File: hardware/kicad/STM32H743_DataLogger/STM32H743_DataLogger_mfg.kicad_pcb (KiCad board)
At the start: 4 copper layers, 160 x 100 mm, 228 parts, among them J1 24VDC_Input, J10 SWD_Debug, J11 USB-C, J12 UART_Debug, J13 BOOT0_Select, J14 TC2050-IDC, J20 AI_CH0, J21 AI_CH1, J22 AI_CH2, J23 AI_CH3, J30 DI_0, J31 DI_1, J32 DI_2, J33 DI_3, J34 DI_4, J35 DI_5, J36 DI_6, J37 DI_7, J40 DO_0, J41 DO_1, J42 DO_2, J43 DO_3, J50 RS485, J51 CAN, J60 J0011D21BNL, J70 SMA_LoRa, J71 U.FL_WiFi, J72 NanoSIM, J73 SMA_LTE, J74 SMA_GNSS, J80 microSD, K1 HF46F-G/5-HS1T, K2 HF46F-G/5-HS1T, K3 HF46F-G/5-HS1T, K4 HF46F-G/5-HS1T, Q1 SI4435DDY, U1 TPS54560, U10 STM32H743VIT6, U2 TLV1117LV33, U20 OPA2376, U21 OPA2376, U3 TPS7A4533, U30 TLP293, U31 ULN2003A, U32 TLP293, U33 TLP293, U34 TLP293, U35 TLP293, U36 TLP293, U37 TLP293, U38 TLP293, U40 ISO3082, U41 ISO1042, U42 NXJ1S0505MC, U43 NXJ1S0505MC, U50 W5500, U60 SX1276, U61 ATWINC1500, U62 SIM7600G-H, U62B RN4870, U63 TPS73641, U64 TPS3823-33, U70 W25Q64JV, U71 AT24C256C, Y1 25MHz, Y2 32.768kHz, Y3 25MHz, Y4 32MHz

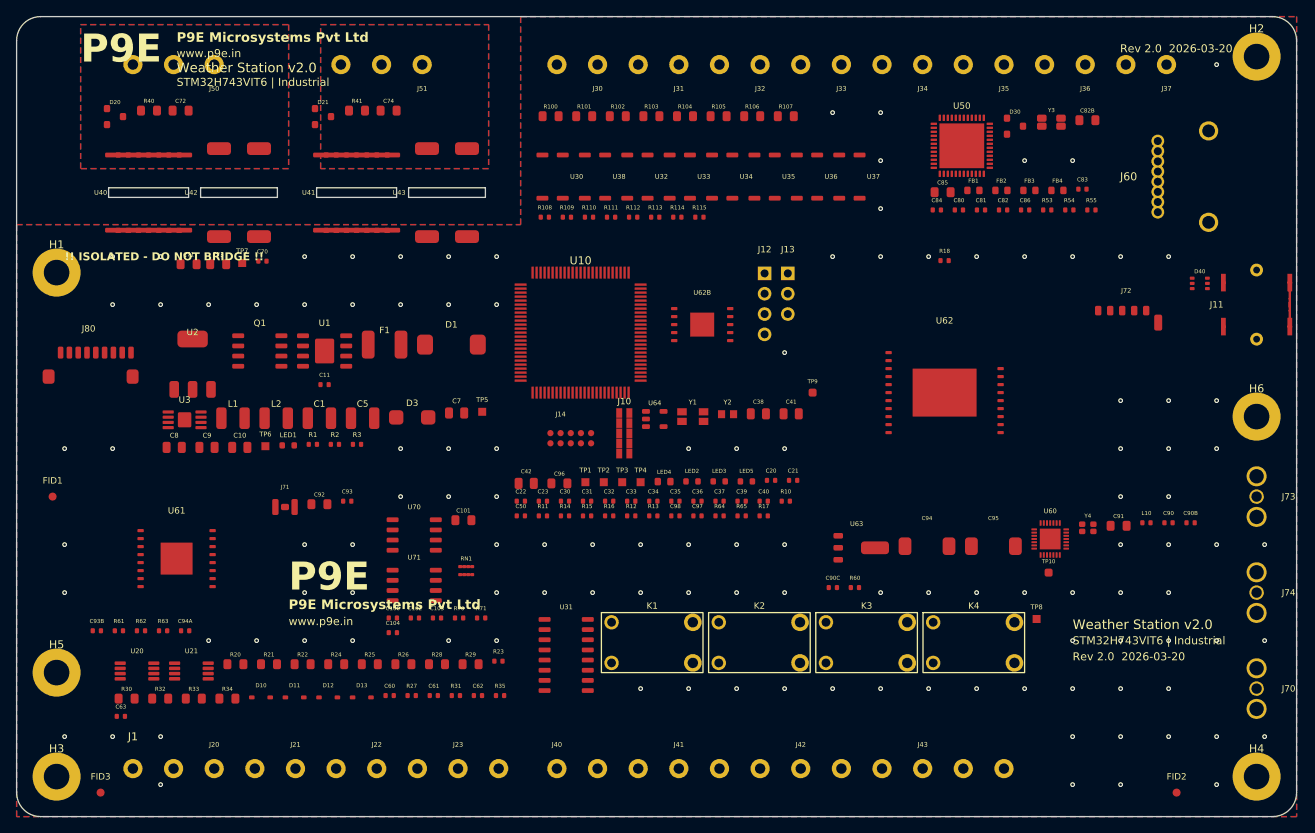
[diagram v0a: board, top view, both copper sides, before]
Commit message: Import the autorouted session; 84% of connections, verified independently
Built a Specctra DSN exporter and a session importer, routed the board
with freerouting, and imported the result: 1520 tracks and 303 vias on
F.Cu / In2.Cu / B.Cu, with In1.Cu left as an unbroken ground plane.

Getting there took three format fixes worth recording. The DSN declared
(resolution um 10) but coordinates were scaled mm->um, so the router saw a
16x10mm board and could place almost nothing; %g emitted scientific
notation for large coordinates, which the parser rejected; and the session
comes back at 100000 units/mm rather than the 10000 the DSN uses, which
imported every track 10x oversized until it was caught by comparing a
track endpoint against its pad.

Via size turned out to be the real routing constraint: at 0.6mm the
autorouter could not stagger a fanout into the 0.5mm-pitch LQFP-100 and
completed under half the board. At 0.45mm/0.25mm with 0.125mm clearance it
gets much further.

Do not trust the router's own completion figure. Freerouting reported "3
unrouted" for this session; walking each net's pads against the imported
copper shows many MCU pins never reached. The real figure is 271 of 322
connections (84%) - 110 nets complete, 35 partial, 10 untouched - and the
45 nets needing work are listed in docs/unrouted_nets.txt.

Also removed 10 segments and vias where freerouting had taken NRST,
RS485_DE and FDCAN1_TX through the isolated corner. The router has no
notion of which nets may enter the field-side pocket, so an incomplete net
is the right trade against a bridged 5kV barrier. Isolation violations are
now zero. The isolator logic pins sit 0.7mm from the notch edge, which is
what invites this - noted that the barrier row should move down ~2mm if it
recurs.

The GND stitching was regenerated after routing rather than before, since
the old grid predated the tracks and would have shorted them.

This routing is superseded once the MCU pinout in 7.8 is corrected, but
the plac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
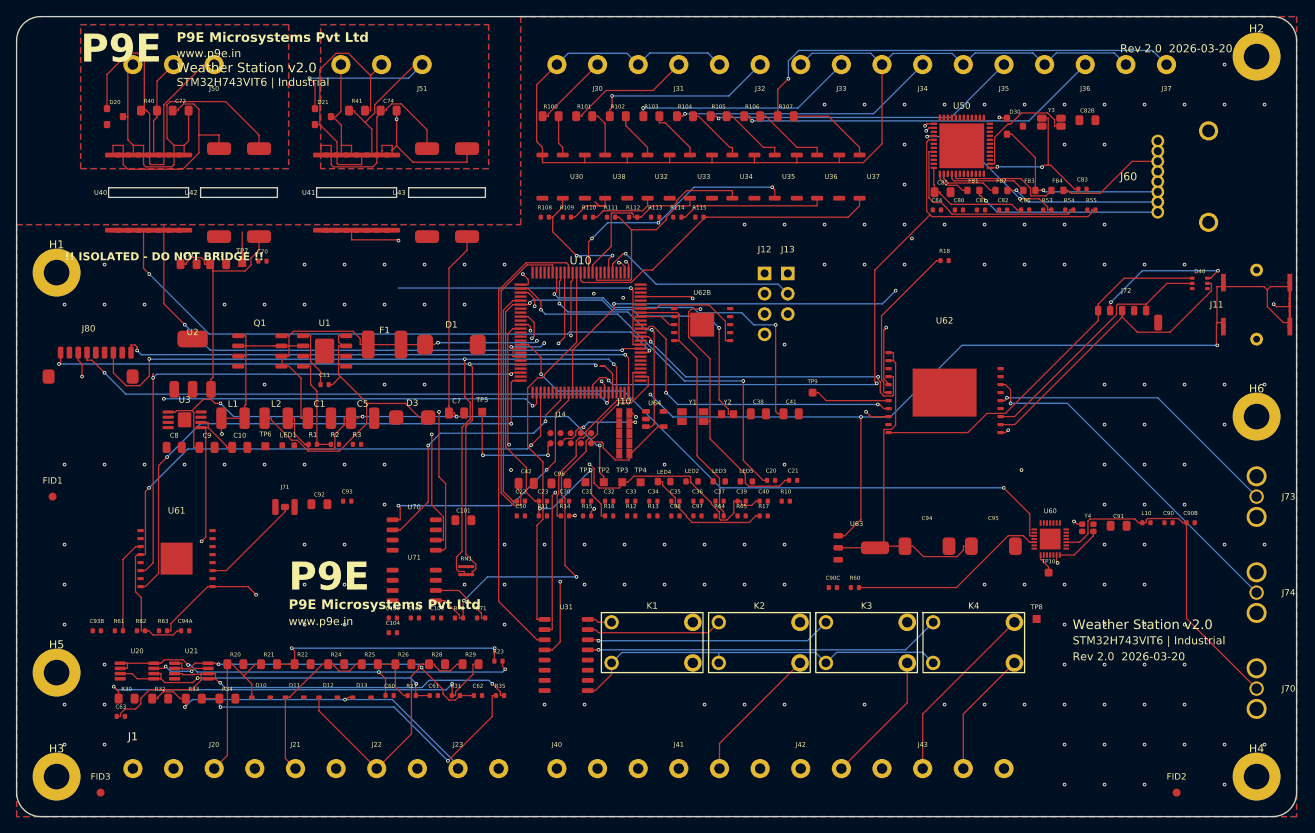
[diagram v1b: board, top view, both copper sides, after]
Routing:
- net +5V: track 0.00 -> 262.8 mm, vias 0 -> 7
- net +24V: track 0.00 -> 223.6 mm, vias 0 -> 4
- net DI_COM: track 0.00 -> 141.7 mm
- net ADC1_CH3: track 0.00 -> 105.2 mm, vias 0 -> 3
- net ADC1_CH0: track 0.00 -> 101.9 mm, vias 0 -> 4
- net SDMMC1_CMD: track 0.00 -> 101.1 mm, vias 0 -> 3
- net SDMMC1_D0: track 0.00 -> 96.3 mm, vias 0 -> 3
- net ETH_INT: track 0.00 -> 92.9 mm, vias 0 -> 2
- net ADC1_CH2: track 0.00 -> 91.5 mm, vias 0 -> 3
- net WIFI_RST: track 0.00 -> 81.9 mm, vias 0 -> 2
- net SPI1_MISO: track 0.00 -> 76.9 mm, vias 0 -> 2
- net +3V3A: track 0.00 -> 75.3 mm, vias 0 -> 4
- net USART2_RX: track 0.00 -> 73.7 mm, vias 0 -> 2
- net SPI2_SCK: track 0.00 -> 73.1 mm, vias 0 -> 2
- net SPI4_SCK: track 0.00 -> 72.4 mm, vias 0 -> 3
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
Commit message: Rebuild the MCU pin assignment from the real LQFP-100 pinout
With KiCad available I could fetch the MCU_ST_STM32H7 symbol library,
which carries the STM32H743VITx pin table generated from the ST datasheet
— the authoritative source that was missing when I flagged this as
blocking. U10's pad-to-net map is rebuilt from it.

Verified against the pins the package fixes, all of which now land
correctly: NRST=14, BOOT0=94, VBAT=6, VDDA/VREF+/VSSA=21/20/19,
VCAP=48/73, VDD=11/27/50/75/100, VSS=10/26/49/74/99. +24V no longer
appears anywhere on the MCU. 90 pins assigned, 10 left spare.

The symbol also carries per-pin alternate-function lists, which resolved
the two conflicts the old notes contained without guesswork:

- UART4_TX moves PA0 -> PB9. PA0 is an ADC1 channel and the four analog
  inputs must stay on PA0-PA3; PB9 was the only free UART4_TX-capable pin.
- UART4_RX moves PC11 -> PB8. PC11 is SDMMC1_D3, and all five
  UART4_RX-capable pins were occupied, so WDT_KICK gave up PB8.
- WDT_KICK moves PB8 -> PD9, displaced by the above. It only drives the
  TPS3823 watchdog input, so any free GPIO serves.
- LORA_RST and GSM_PWR_KEY move off PC2/PC3 to PB10/PB11: on the 100-pin
  package those are the dual-pad PC2_C/PC3_C direct-analog variants, and
  both signals are plain GPIO resets that should not depend on the analog
  switch.

SD_CD was never assigned in the old notes at all; it is now on PD15.

These four reassignments change the firmware pin map and need sign-off.
They are recorded in design spec 7.8 and in the MCU sheet annotation,
which now carries the full signal-to-pin table instead of port names.

All 157 nets still reach at least two pads. The DO NOT FABRICATE banner
is removed. The old routing was cut for the previous pinout and has been
discarded; re-routing is in progress.

Co-Authored-By: Claude Opus 5 <noreply@anthropic.com>
Claude-Session: https://claude.ai/code/session_01XsiZ6LJT6X46LKY8yEbRbx
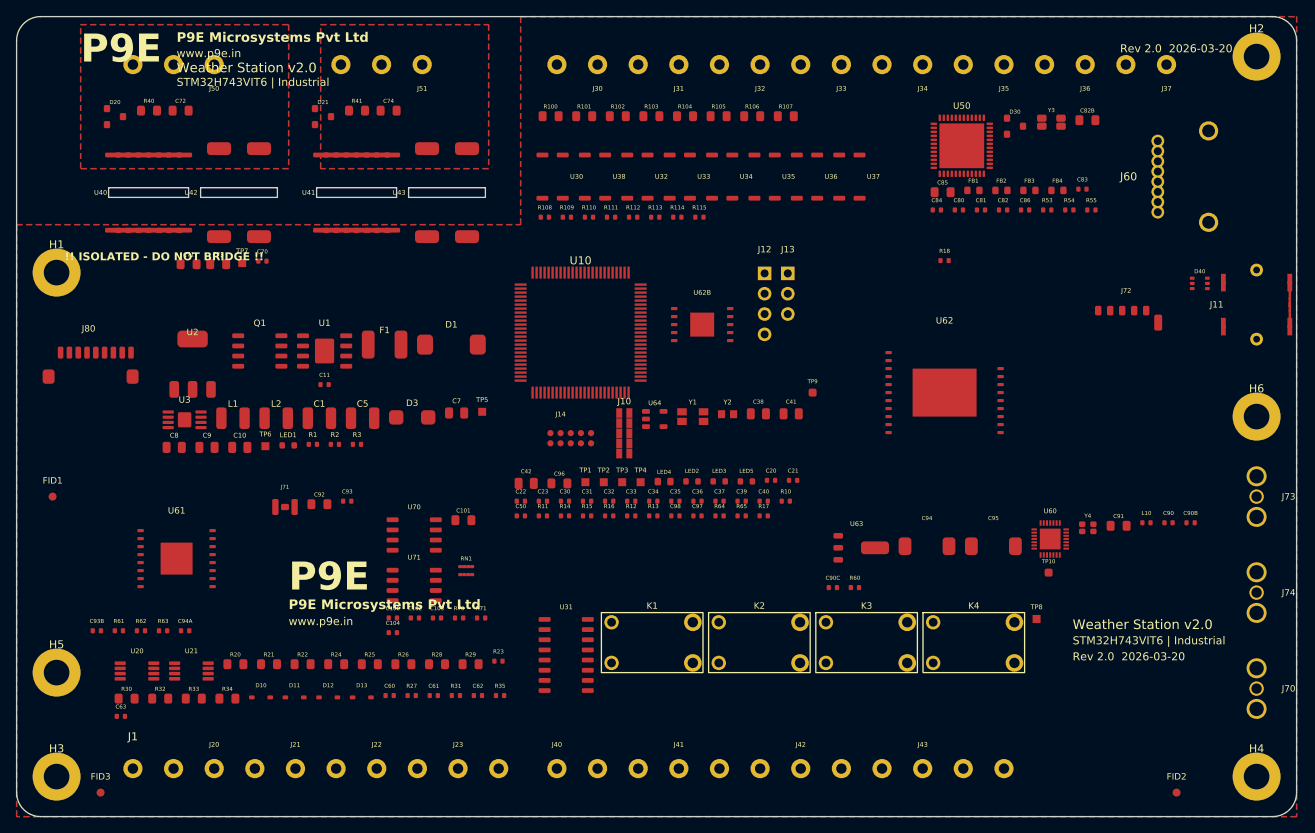
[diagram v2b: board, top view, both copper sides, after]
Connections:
- U10 pad 1: +24V -> SPI4_SCK
- U10 pad 10: ADC1_CH1 -> GND
- U10 pad 11: ADC1_CH2 -> +3V3
- U10 pad 12: ADC1_CH3 -> HSE_IN
- U10 pad 13: +3V3A -> HSE_OUT
- U10 pad 14: GND -> NRST
- U10 pad 15: SPI1_SCK -> WIFI_RST
- U10 pad 16: SPI1_MISO -> (no net)
- U10 pad 17: SPI1_MOSI -> (no net)
- U10 pad 18: NSS_LORA -> (no net)
- U10 pad 19: LORA_DIO0 -> GND
- U10 pad 2: HSE_IN -> ETH_RST
- U10 pad 20: LORA_RST -> +3V3A
- U10 pad 21: +3V3 -> +3V3A
- U10 pad 22: GND -> ADC1_CH0
- U10 pad 23: SPI2_SCK -> ADC1_CH1
- U10 pad 24: SPI2_MISO -> ADC1_CH2
- U10 pad 25: SPI2_MOSI -> ADC1_CH3
- U10 pad 26: NSS_WIFI -> GND
- U10 pad 27: WIFI_EN -> +3V3
- U10 pad 28: WIFI_RST -> NSS_LORA
- U10 pad 29: WIFI_IRQ -> SPI1_SCK
- U10 pad 3: HSE_OUT -> NSS_ETH
- U10 pad 30: +3V3 -> SPI1_MISO
- U10 pad 31: GND -> (no net)
- U10 pad 32: SPI3_SCK -> (no net)
- U10 pad 33: SPI3_MISO -> (no net)
- U10 pad 34: SPI3_MOSI -> ETH_INT
- U10 pad 35: NSS_FLASH -> WIFI_EN
- U10 pad 36: SPI4_SCK -> SPI3_MOSI
- U10 pad 37: SPI4_MISO -> UART7_RX
- U10 pad 38: SPI4_MOSI -> UART7_TX
- U10 pad 39: NSS_ETH -> DI_4
- U10 pad 4: NRST -> SPI4_MISO
- U10 pad 40: ETH_RST -> DI_5
- U10 pad 41: ETH_INT -> DI_6
- U10 pad 42: SDMMC1_D0 -> DI_7
- U10 pad 43: SDMMC1_D1 -> DO_0
- U10 pad 44: SDMMC1_D2 -> DO_1
- U10 pad 45: SDMMC1_D3 -> DO_2
- U10 pad 46: SDMMC1_CLK -> LORA_RST
- U10 pad 47: SDMMC1_CMD -> GSM_PWR_KEY
- U10 pad 48: +3V3 -> VCAP1
- U10 pad 5: LSE_IN -> SPI4_MOSI
- U10 pad 50: SD_CD -> +3V3
- U10 pad 51: I2C1_SCL -> NSS_WIFI
- U10 pad 52: I2C1_SDA -> SPI2_SCK
- U10 pad 53: USART1_TX -> SPI2_MISO
- U10 pad 54: USART1_RX -> SPI2_MOSI
- U10 pad 55: +3V3 -> (no net)
- U10 pad 56: GND -> WDT_KICK
- U10 pad 57: USART2_TX -> WIFI_IRQ
- U10 pad 58: USART2_RX -> GSM_STATUS
- U10 pad 59: RS485_DE -> BLE_RST
- U10 pad 6: LSE_OUT -> +3V3
- U10 pad 60: FDCAN1_TX -> BLE_STATUS
- U10 pad 61: FDCAN1_RX -> DO_3
- U10 pad 62: UART4_TX -> SD_CD
- U10 pad 63: UART4_RX -> (no net)
- U10 pad 64: GSM_PWR_KEY -> (no net)
- U10 pad 65: GSM_STATUS -> SDMMC1_D0
- U10 pad 66: UART7_TX -> SDMMC1_D1
- U10 pad 67: UART7_RX -> (no net)
- U10 pad 68: BLE_RST -> USART1_TX
- U10 pad 69: BLE_STATUS -> USART1_RX
- U10 pad 7: GND -> LORA_DIO0
- U10 pad 70: +3V3 -> USB_DM
- U10 pad 71: GND -> USB_DP
- U10 pad 72: USB_DM -> SWDIO
- U10 pad 73: USB_DP -> VCAP2
- U10 pad 74: +3V3 -> GND
- U10 pad 75: GND -> +3V3
- U10 pad 76: SWDIO -> SWCLK
- U10 pad 77: SWCLK -> NSS_FLASH
- U10 pad 78: +3V3 -> SDMMC1_D2
- U10 pad 79: GND -> SDMMC1_D3
- U10 pad 8: +3V3 -> LSE_IN
- U10 pad 80: BOOT0 -> SDMMC1_CLK
- U10 pad 81: DI_0 -> FDCAN1_RX
- U10 pad 82: DI_1 -> FDCAN1_TX
- U10 pad 83: DI_2 -> SDMMC1_CMD
- U10 pad 84: DI_3 -> DI_0
- U10 pad 85: DI_4 -> RS485_DE
- U10 pad 86: DI_5 -> USART2_TX
- U10 pad 87: DI_6 -> USART2_RX
- U10 pad 88: DI_7 -> DI_1
- U10 pad 89: DO_0 -> SPI3_SCK
- U10 pad 9: ADC1_CH0 -> LSE_OUT
- U10 pad 90: DO_1 -> SPI3_MISO
- U10 pad 91: DO_2 -> SPI1_MOSI
- U10 pad 92: DO_3 -> I2C1_SCL
- U10 pad 93: WDT_KICK -> I2C1_SDA
- U10 pad 94: VCAP1 -> BOOT0
- U10 pad 95: VCAP2 -> UART4_RX
- U10 pad 96: +3V3 -> UART4_TX
- U10 pad 97: GND -> DI_2
- U10 pad 98: +3V3 -> DI_3
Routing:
- net +5V: track 262.8 -> 0.00 mm, vias 7 -> 0
- net +24V: track 223.6 -> 0.00 mm, vias 4 -> 0
- net DI_COM: track 141.7 -> 0.00 mm
- net ADC1_CH3: track 105.2 -> 0.00 mm, vias 3 -> 0
- net ADC1_CH0: track 101.9 -> 0.00 mm, vias 4 -> 0
- net SDMMC1_CMD: track 101.1 -> 0.00 mm, vias 3 -> 0
- net SDMMC1_D0: track 96.3 -> 0.00 mm, vias 3 -> 0
- net ETH_INT: track 92.9 -> 0.00 mm, vias 2 -> 0
- net ADC1_CH2: track 91.5 -> 0.00 mm, vias 3 -> 0
- net WIFI_RST: track 81.9 -> 0.00 mm, vias 2 -> 0
- net SPI1_MISO: track 76.9 -> 0.00 mm, vias 2 -> 0
- net +3V3A: track 75.3 -> 0.00 mm, vias 4 -> 0
- net USART2_RX: track 73.7 -> 0.00 mm, vias 2 -> 0
- net SPI2_SCK: track 73.1 -> 0.00 mm, vias 2 -> 0
- net SPI4_SCK: track 72.4 -> 0.00 mm, vias 3 -> 0
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
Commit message: Verify every IC against its datasheet pinout; rebuild three, add missing parts
The MCU turned out not to be the only placeholder. With the symbol
libraries available I checked each IC's footprint wiring against the pin
names its datasheet-derived KiCad symbol gives — if a pin the datasheet
calls VDD is not on a supply net, the map was not derived from the
datasheet. Three ICs failed and are rebuilt:

- U50 W5500 had SPI on the Ethernet differential pins and supplies and
  grounds on ten wrong pads. Rebuilt from the 48-pin pinout: SPI on
  32-37, TX/RX pairs on 1/2/5/6, PMODE2..0 grounded for all-capable
  auto-negotiation.
- U40 ISO3082 had the receiver and driver swapped, the bus A/B pair one
  pin out, and GND2 carrying the isolated 5V supply.
- U1 TPS54560 had the switch node on pins 7 and 8, shorting SW to GND,
  and FB off pin 5.

Verifying the W5500 also showed three datasheet-required parts were never
placed: R56 (12.4k on EXRES1, sets transmit bias current), C87 (4.7uF on
TOCAP) and C88 (100nF on VBG). All three added.

Two ICs cannot be verified and are recorded as such rather than guessed
at. U60 is worse than a wiring error: the footprint is QFN-28 4x4mm on
0.4mm pitch, but SX1276IMLTRT is 6x6mm on 0.65mm pitch — the wrong
package outline entirely. U3's part is the DGN (MSOP-8-EP) variant and
the library only has KTT (TO-263-5), a different pinout, so it cannot
stand in. Six more ICs have no symbol at all and show the same sequential
pattern; they should be assumed wrong until checked.

Still open on the buck: EN, RT/CLK and COMP have no components on them.
RT/CLK sets the switching frequency and COMP is the compensation network,
so U1 will not regulate as drawn.

Also corrected twelve wrong schematic lib_ids against the real libraries;
35 of 44 now resolve, and the nine that need symbols drawn are listed in
docs/Schematic_Symbol_Audit.md.

BOM now 123 line items / 222 components; netlist 160 nets, all reaching
at least two pads.

Co-Authored-By: Claude O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
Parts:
- added C87: 4.7uF, Capacitor_SMD:C_0805_2012Metric, F.Cu at (125.0, 17.5)
- added C88: 100nF, Capacitor_SMD:C_0402_1005Metric, F.Cu at (112.0, 18.0)
- added R56: 12.4k 1%, Resistor_SMD:R_0402_1005Metric, F.Cu at (112.0, 16.0)
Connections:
- U1 pad 4: VFB -> (no net)
- U1 pad 5: GND -> VFB
- U1 pad 6: GND -> (no net)
- U1 pad 7: VBUCK_SW -> GND
- U40 pad 11: RS485_A -> (no net)
- U40 pad 12: RS485_B -> RS485_A
- U40 pad 13: RS485_ISO_GND -> RS485_B
- U40 pad 14: RS485_ISO_GND -> (no net)
- U40 pad 15: RS485_ISO_VCC -> RS485_ISO_GND
- U40 pad 3: USART2_TX -> USART2_RX
- U40 pad 4: USART2_RX -> RS485_DE
- U40 pad 6: RS485_DE -> USART2_TX
- U50 pad 1: SPI4_SCK -> ETH_TXN
- U50 pad 10: +3V3 -> W5500_EXRES
- U50 pad 11: GND -> +3V3
- U50 pad 12: W5500_1V8OUT -> (no net)
- U50 pad 13: ETH_TXP -> (no net)
- U50 pad 14: ETH_TXN -> GND
- U50 pad 15: GND -> +3V3
- U50 pad 16: ETH_RXP -> GND
- U50 pad 17: ETH_RXN -> +3V3
- U50 pad 18: GND -> W5500_VBG
- U50 pad 19: +3V3 -> GND
- U50 pad 2: SPI4_MISO -> ETH_TXP
- U50 pad 20: GND -> W5500_TOCAP
- U50 pad 22: GND -> W5500_1V8OUT
- U50 pad 23: +3V3 -> (no net)
- U50 pad 24: GND -> (no net)
- U50 pad 25: W5500_XTAL1 -> (no net)
- U50 pad 26: W5500_XTAL2 -> (no net)
- U50 pad 27: GND -> (no net)
- U50 pad 3: SPI4_MOSI -> GND
- U50 pad 30: +3V3 -> W5500_XTAL1
- U50 pad 31: GND -> W5500_XTAL2
- U50 pad 32: +3V3 -> NSS_ETH
- U50 pad 33: GND -> SPI4_SCK
- U50 pad 34: +3V3 -> SPI4_MISO
- U50 pad 35: GND -> SPI4_MOSI
- U50 pad 36: +3V3 -> ETH_INT
- U50 pad 37: GND -> ETH_RST
- U50 pad 38: +3V3 -> (no net)
- U50 pad 39: GND -> (no net)
- U50 pad 4: NSS_ETH -> +3V3
- U50 pad 40: +3V3 -> (no net)
- U50 pad 41: GND -> (no net)
- U50 pad 42: +3V3 -> (no net)
- U50 pad 44: +3V3 -> GND
- U50 pad 46: +3V3 -> (no net)
- U50 pad 47: GND -> (no net)
- U50 pad 48: +3V3 -> GND
- U50 pad 5: ETH_INT -> ETH_RXN
- U50 pad 6: +3V3 -> ETH_RXP
- U50 pad 7: GND -> (no net)
- U50 pad 8: ETH_RST -> +3V3
